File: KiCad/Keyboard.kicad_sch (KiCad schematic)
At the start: 70 parts, among them J1 USB_C_Receptacle, SW1 SW_Push, SW10 SW_Push, SW13 SW_Push, SW14 SW_Push, SW15 SW_Push, SW16 SW_Push, SW19 SW_Push, SW2 SW_Push, SW20 SW_Push, SW21 SW_Push, SW22 SW_Push, SW25 SW_Push, SW26 SW_Push, SW27 SW_Push, SW29 SW_Push, SW3 SW_Push, SW30 SW_Push, SW31 SW_Push, SW32 SW_Push, SW33 SW_Push, SW34 SW_Push, SW35 SW_Push, SW36 SW_Push, SW39 SW_Push, SW4 SW_Push, SW5 SW_Push, SW7 SW_Push, SW8 SW_Push, SW9 SW_Push, U1 ESP32-C6-MINI-1, U2 USBLC6-2SC6

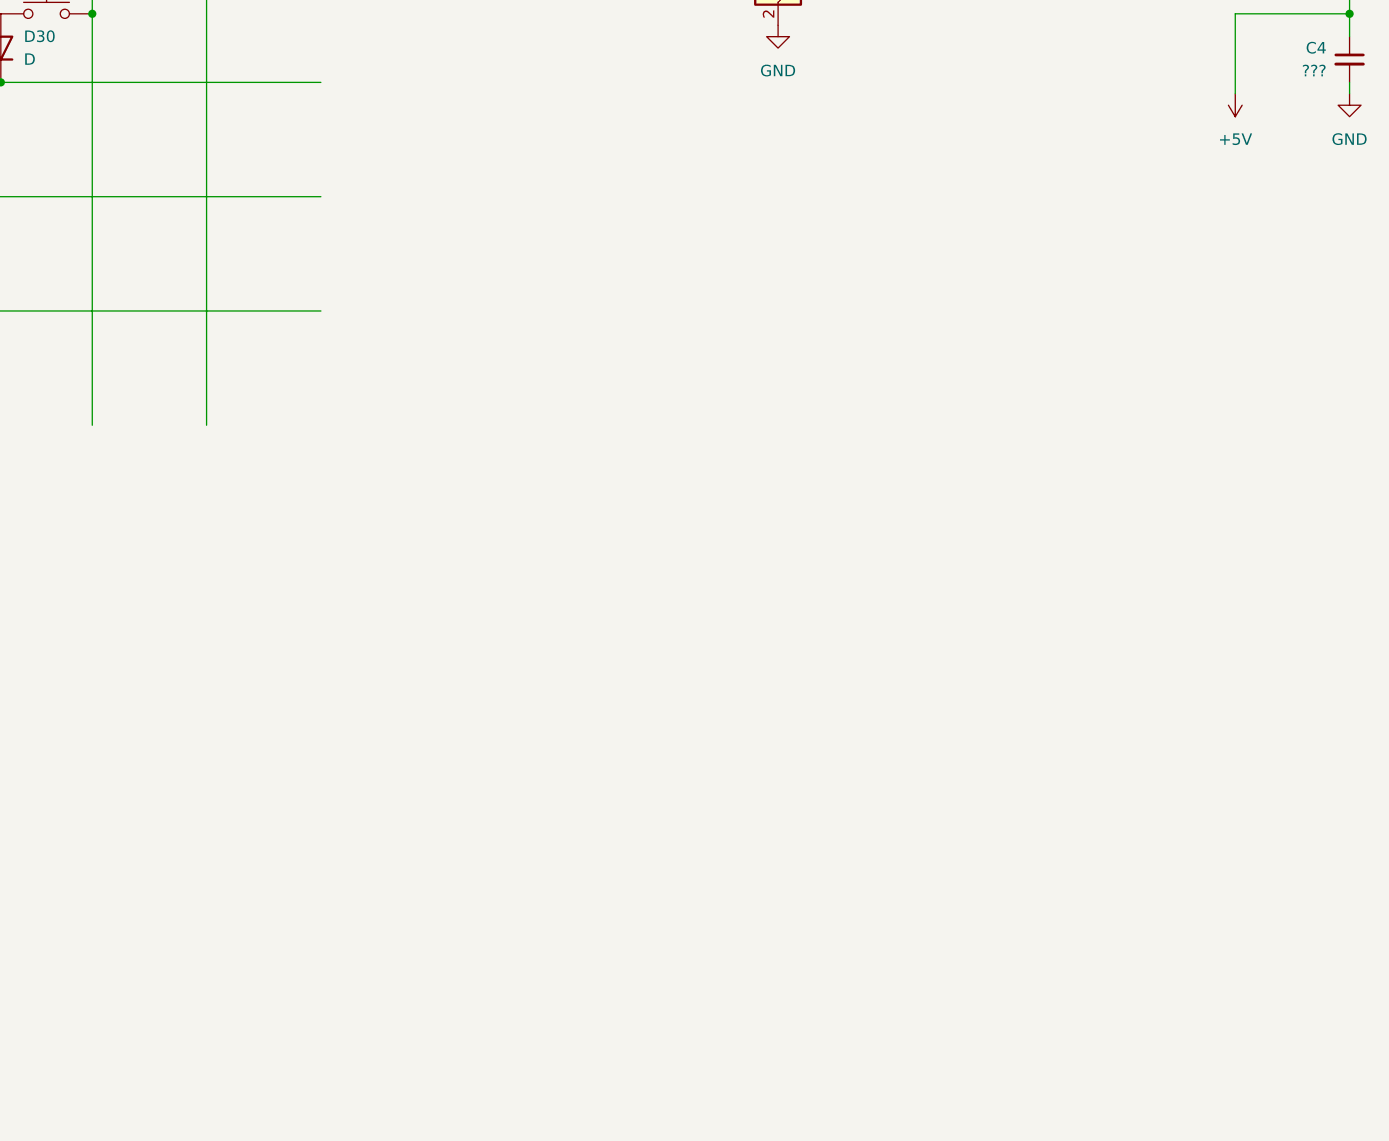
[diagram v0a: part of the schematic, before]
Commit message: Buck-boost converter hookup + WIP charger
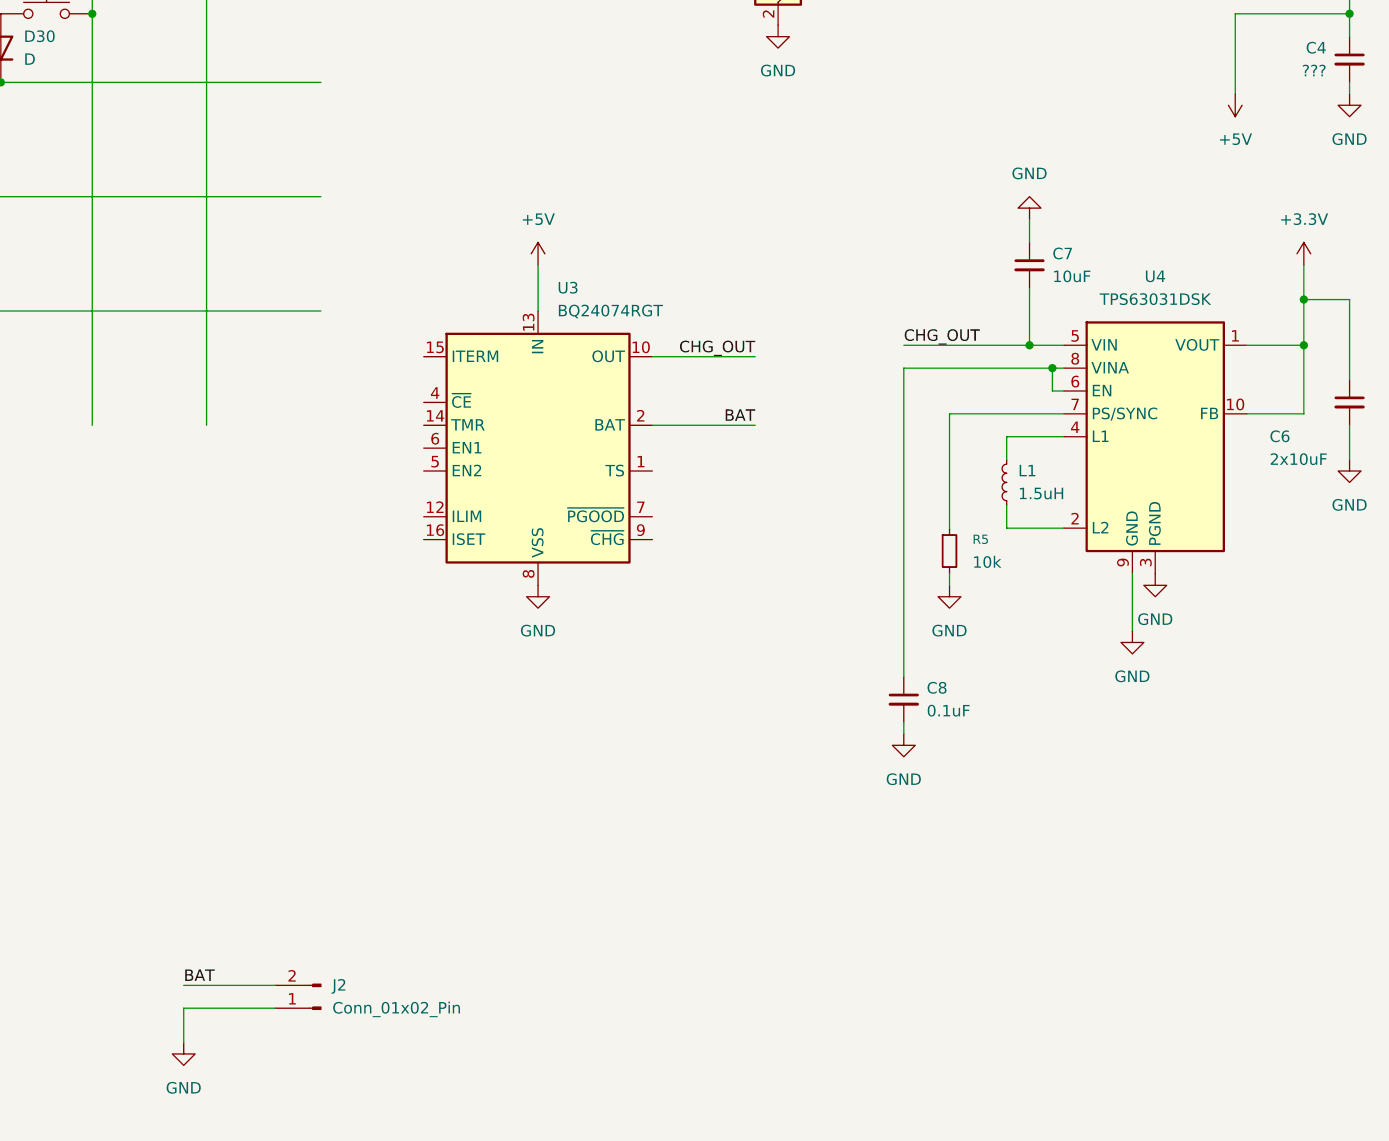
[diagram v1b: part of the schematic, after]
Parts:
- added C6: 2x10uF, symbol Device:C_Small
- added C7: 10uF, symbol Device:C_Small
- added C8: 0.1uF, symbol Device:C_Small
- added J2: Conn_01x02_Pin, symbol Connector:Conn_01x02_Pin
- added L1: 1.5uH, symbol Device:L_Small
- added R5: 10k, symbol Device:R_Small
- added U3: BQ24074RGT, Package_DFN_QFN:VQFN-16-1EP_3x3mm_P0.5mm_EP1.6x1.6mm, symbol Battery_Management:BQ24074RGT
- added U4: TPS63031DSK, Package_SON:WSON-10-1EP_2.5x2.5mm_P0.5mm_EP1.2x2mm, symbol Regulator_Switching:TPS63031DSK
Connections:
- net +3.3V: now also C6.1, U4.1 (VOUT), U4.10 (FB)
- net +5V: now also U3.13 (IN)
- net GND: now also C6.2, C7.1, C8.2, J2.1 (Pin_1), R5.2, U3.17 (VSS), U3.8 (VSS), U4.11 (PGND), U4.3 (PGND), U4.9 (GND)
- new net: L1.1, U4.2 (L2)
- new net: L1.2, U4.4 (L1)
- new net: C8.1, U4.6 (EN), U4.8 (VINA)
- new net: R5.1, U4.7 (PS/SYNC)
- new net BAT: J2.2 (Pin_2), U3.2 (BAT), U3.3 (BAT)
- new net CHG_OUT: C7.2, U3.10 (OUT), U3.11 (OUT), U4.5 (VIN)

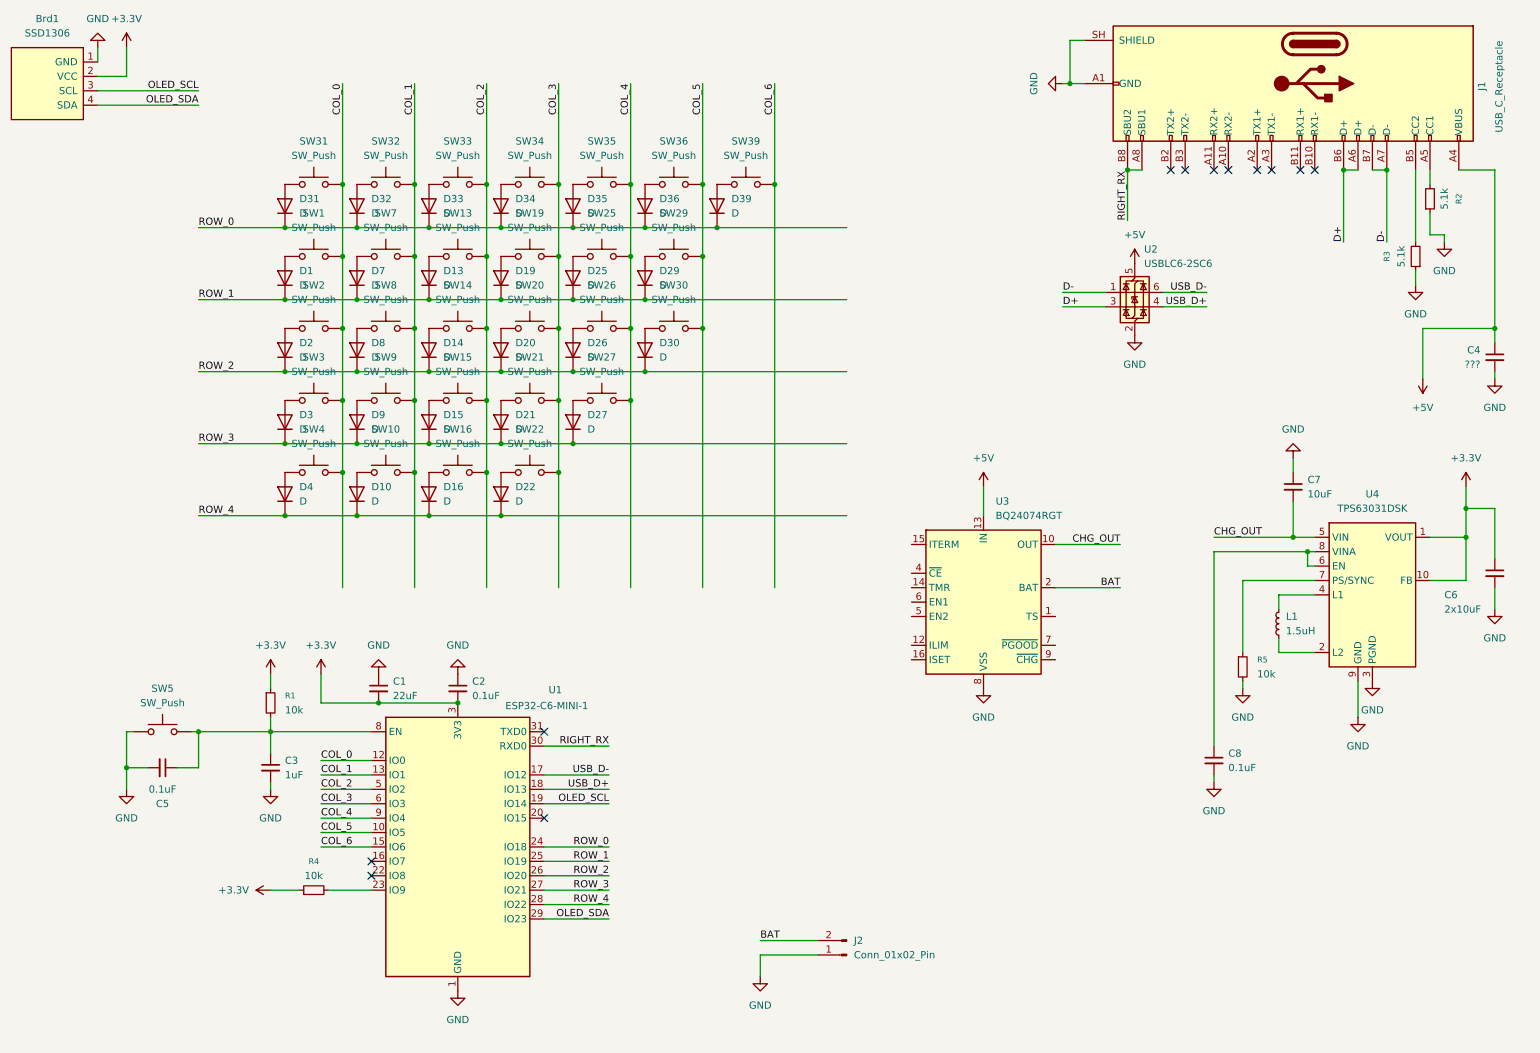
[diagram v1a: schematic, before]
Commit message: Charger hookup
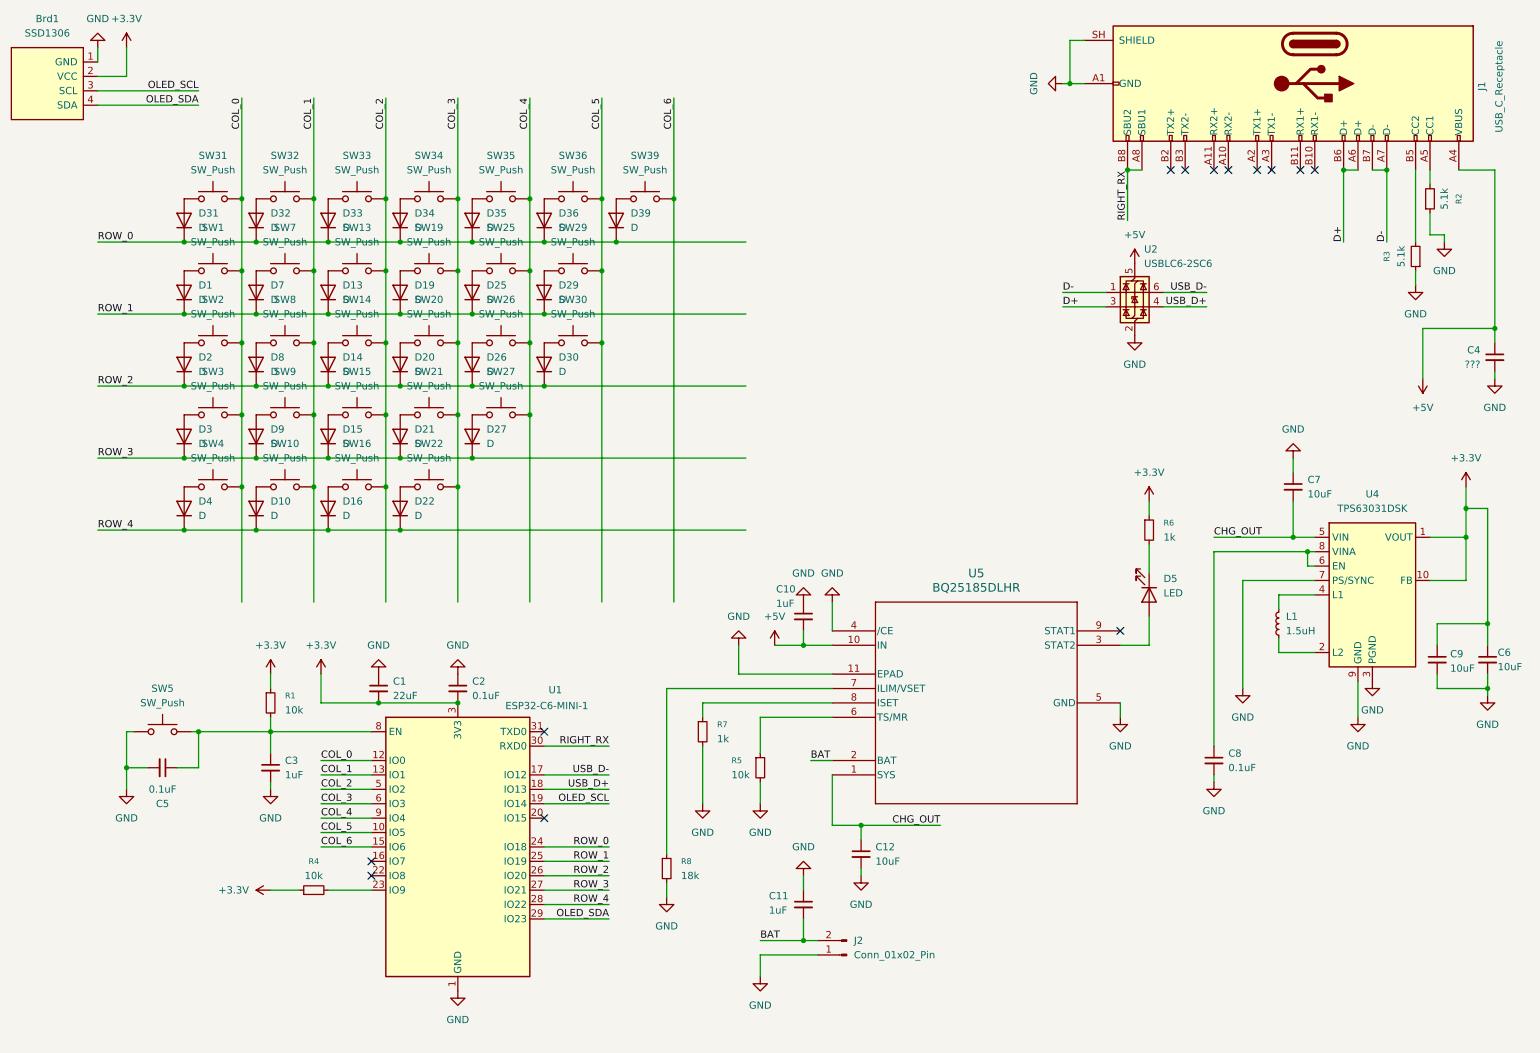
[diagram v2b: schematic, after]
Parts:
- removed U3: BQ24074RGT, Package_DFN_QFN:VQFN-16-1EP_3x3mm_P0.5mm_EP1.6x1.6mm, symbol Battery_Management:BQ24074RGT
- added C10, C11: 1uF, symbol Device:C_Small
- added C12, C9: 10uF, symbol Device:C_Small
- added D5: LED, symbol Device:LED
- added R6, R7: 1k, symbol Device:R_Small
- added R8: 18k, symbol Device:R_Small
- added U5: BQ25185DLHR, WSON10_DLH_TEX, symbol BQ25185:BQ25185DLHR
- C6: value 2x10uF -> 10uF
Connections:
- net +3.3V: now also C9.1, R6.1
- net +5V: now also C10.2, U5.10 (IN)
- net BAT: now also C11.2, U5.2 (BAT)
- net CHG_OUT: now also C12.1, U5.1 (SYS)
- net GND: now also U4.7 (PS/SYNC), C10.1, C11.1, C12.2, C9.2, R7.2, R8.2, U5.11 (EPAD), U5.4 (/CE), U5.5 (GND)
- net at R5.1: now also U5.6 (TS/MR); no longer U4.7 (PS/SYNC)
- new net: D5.1 (K), R6.2
- new net: D5.2 (A), U5.3 (STAT2)
- new net: R7.1, U5.8 (ISET)
- new net: R8.1, U5.7 (ILIM/VSET)
- no-connect marks 12 -> 13
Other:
- moved on the sheet: C6, D1, D10, D13, D14, D15, D16, D19, D2, D20, D21, D22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

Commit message: ERC feedback
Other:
- moved on the sheet: C11

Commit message: Label all switches and switch diodes
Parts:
- Brd1: footprint (none) -> SSD1306:128x64OLED
- D1: renamed from D31; value D -> D_SW_TICK
- D10: renamed from D9; value D -> D_SW_Z
- D11: renamed from D10; value D -> D_SW_SUPER
- D12: renamed from D33; value D -> D_SW_2
- D13: value D -> D_SW_W
- D14: value D -> D_SW_S
- D15: value D -> D_SW_X
- D16: value D -> D_SW_ALT
- D17: renamed from D34; value D -> D_SW_3
- D18: renamed from D19; value D -> D_SW_E
- D19: renamed from D20; value D -> D_SW_D
- D2: renamed from D1; value D -> D_SW_TAB
- D20: renamed from D21; value D -> D_SW_C
- D21: renamed from D22; value D -> D_SW_SPACE
- D22: renamed from D35; value D -> D_SW_4
- D23: renamed from D25; value D -> D_SW_R
- D24: renamed from D26; value D -> D_SW_F
- D25: renamed from D27; value D -> D_SW_V
- D26: renamed from D36; value D -> D_SW_5
- D27: renamed from D29; value D -> D_SW_T
- D28: renamed from D30; value D -> D_SW_G
- D29: renamed from D39; value D -> D_SW_6
- D3: renamed from D2; value D -> D_SW_CAPS
- D4: renamed from D3; value D -> D_SW_SHIFT
- D6: renamed from D4; value D -> D_SW_CTRL
- D7: renamed from D32; value D -> D_SW_1
- D8: renamed from D7; value D -> D_SW_Q
- D9: renamed from D8; value D -> D_SW_A
- SW1: renamed from SW5; value SW_Push -> SW5
- SW10: renamed from SW9; value SW_Push -> SW_Z
- SW11: renamed from SW10; value SW_Push -> SW_SUPER
- SW12: renamed from SW33; value SW_Push -> SW_2
- SW13: value SW_Push -> SW_W
- SW14: value SW_Push -> SW_S
- SW15: value SW_Push -> SW_X
- SW16: value SW_Push -> SW_ALT
- SW17: renamed from SW34; value SW_Push -> SW_3
- SW18: renamed from SW19; value SW_Push -> SW_E
- SW19: renamed from SW20; value SW_Push -> SW_D
- SW2: renamed from SW31; value SW_Push -> SW_TICK
- SW20: renamed from SW21; value SW_Push -> SW_C
- SW21: renamed from SW22; value SW_Push -> SW_SPACE
- SW22: renamed from SW35; value SW_Push -> SW_4
- SW23: renamed from SW25; value SW_Push -> SW_R
- SW24: renamed from SW26; value SW_Push -> SW_F
- SW25: renamed from SW27; value SW_Push -> SW_V
- SW26: renamed from SW36; value SW_Push -> SW_5
- SW27: renamed from SW29; value SW_Push -> SW_T
- SW28: renamed from SW30; value SW_Push -> SW_G
- SW29: renamed from SW39; value SW_Push -> SW_6
- SW3: renamed from SW1; value SW_Push -> SW_TAB
- SW4: renamed from SW2; value SW_Push -> SW_CAPS
- SW5: renamed from SW3; value SW_Push -> SW_SHIFT
- SW6: renamed from SW4; value SW_Push -> SW_CTRL
- SW7: renamed from SW32; value SW_Push -> SW_1
- SW8: renamed from SW7; value SW_Push -> SW_Q
- SW9: renamed from SW8; value SW_Push -> SW_A
- U5: footprint WSON10_DLH_TEX -> BQ25185DLHR:WSON10_DLH_TEX
